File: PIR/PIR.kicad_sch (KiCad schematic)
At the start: 31 parts, among them J1 FLASH, J2 PIR, J3 BUS, J4 Conn_01x04_Socket, Q1 BC846, Q2 BC846, Q3 BC857, SW1 tamper switch, U1 AP63203WU, U2 WT8266-S1

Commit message: upgrades people, upgrades!
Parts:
- added TP8: TestPoint, TestPoint:TestPoint_Pad_1.5x1.5mm, symbol Connector:TestPoint
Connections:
- net +3.3V: now also TP8.1

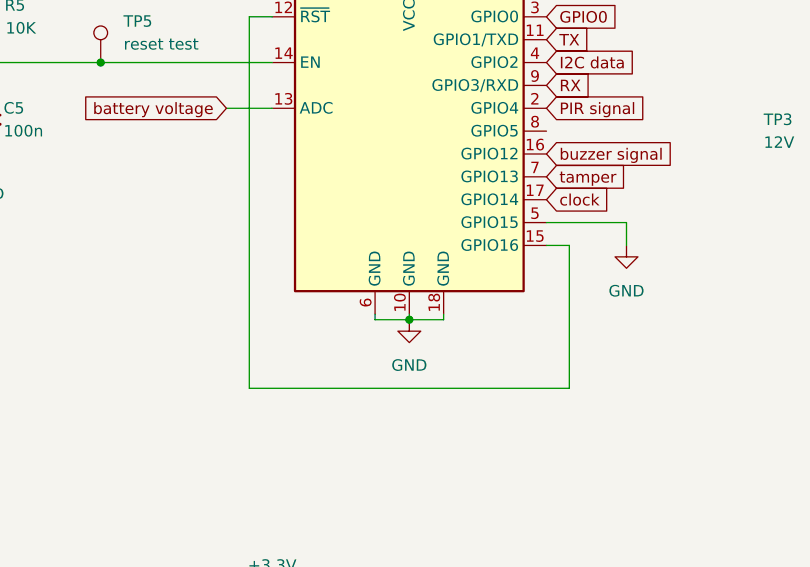
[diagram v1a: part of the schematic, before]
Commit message: Update symbol and footprint of WT8266
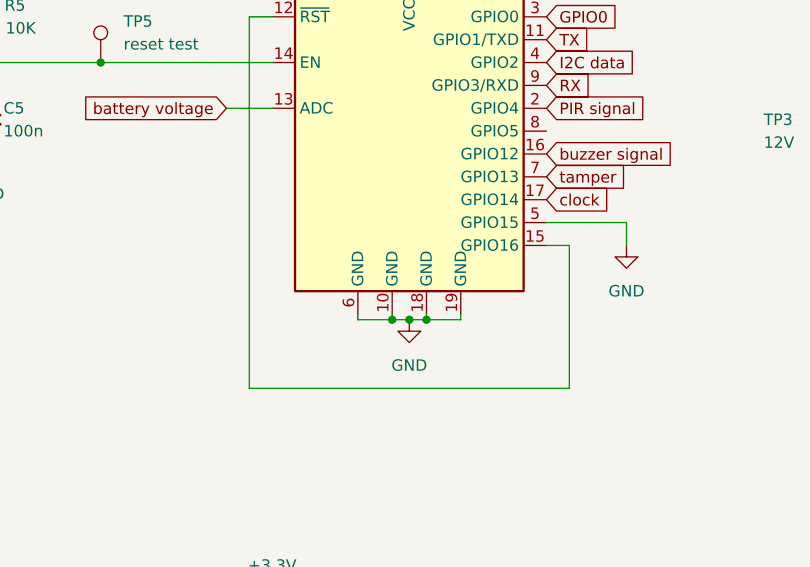
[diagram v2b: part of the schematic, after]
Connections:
- net GND: now also U2.19 (GND)
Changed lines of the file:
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@@
     (company "Radim Kolář, Tomáš Bezányi")
   )
+  (junction (at 94.615 102.235) (diameter 0) (color 0 0 0 0)
+  )
   (junction (at 199.39 121.92) (diameter 0) (color 0 0 0 0)
   )
@@
   (junction (at 144.78 80.01) (diameter 0) (color 0 0 0 0)
   )
+  (junction (at 90.805 102.235) (diameter 0) (color 0 0 0 0)
+  )
   (junction (at 152.4 80.01) (diameter 0) (color 0 0 0 0)
   )
@@
   (junction (at 204.47 82.55) (diameter 0) (color 0 0 0 0)
   )
-  (wire (pts (xy 92.71 101.6) (xy 92.71 102.235))
-    (stroke (width 0) (type default))
-  )
   (wire (pts (xy 160.02 85.09) (xy 152.4 85.09))
     (stroke (width 0) (type default))
@@
     (stroke (width 0) (type default))
   )
+  (wire (pts (xy 90.805 101.6) (xy 90.805 102.235))
+    (stroke (width 0) (type default))
+  )
   (wire (pts (xy 204.47 90.17) (xy 213.36 90.17))
     (stroke (width 0) (type default))
@@
     (stroke (width 0) (type default))
   )
-  (wire (pts (xy 88.9 102.235) (xy 92.71 102.235))
+  (wire (pts (xy 86.995 102.235) (xy 90.805 102.235))
     (stroke (width 0) (type default))
   )
@@
     (stroke (width 0) (type default))
   )
+  (wire (pts (xy 98.425 102.235) (xy 98.425 101.6))
+    (stroke (width 0) (type default))
+  )
   (wire (pts (xy 260.35 40.64) (xy 257.81 40.64))
     (stroke (width 0) (type default))
   )
+  (wire (pts (xy 94.615 102.235) (xy 98.425 102.235))
+    (stroke (width 0) (type default))
+  )
+  (wire (pts (xy 90.805 102.235) (xy 92.71 102.235))
+    (stroke (width 0) (type default))
+  )
   (wire (pts (xy 144.78 80.01) (xy 152.4 80.01))
     (stroke (width 0) (type default))
@@
     (stroke (width 0) (type default))
   )
+  (wire (pts (xy 86.995 102.235) (xy 86.995 101.6))
+    (stroke (width 0) (type default))
+  )
   (wire (pts (xy 204.47 82.55) (xy 213.36 82.55))
     (stroke (width 0) (type default))
@@
     (stroke (width 0) (type default))
   )
+  (wire (pts (xy 94.615 101.6) (xy 94.615 102.235))
+    (stroke (width 0) (type default))
+  )
   (wire (pts (xy 199.39 82.55) (xy 199.39 85.09))
     (stroke (width 0) (type default))
@@
     (stroke (width 0) (type default))
   )
-  (wire (pts (xy 92.71 102.235) (xy 96.52 102.235))
+  (wire (pts (xy 92.71 102.235) (xy 94.615 102.235))
     (stroke (width 0) (type default))
   )
@@
     (stroke (width 0) (type default))
   )
-  (wire (pts (xy 96.52 101.6) (xy 96.52 102.235))
-    (stroke (width 0) (type default))
-  )
   (wire (pts (xy 257.81 40.64) (xy 257.81 48.26))
     (stroke (width 0) (type default))
@@
   )
   (wire (pts (xy 242.57 85.09) (xy 264.16 85.09))
-    (stroke (width 0) (type default))
-  )
-  (wire (pts (xy 88.9 101.6) (xy 88.9 102.235))
     (stroke (width 0) (type default))
   )
@@
       (effects (font (size 1.27 1.27)) hide)
     )
-    (property "Datasheet" "https://botland.cz/index.php?controller=attachment&id_attachment=1796" (at 83.82 81.28 0)
+    (property "Datasheet" "https://web.archive.org/web/20230921181528id_/http://ttcnc.co.kr/wp-content/uploads/2021/05/WT8266-S1-DataSheet-V2.5.pdf" (at 83.82 81.28 0)
       (effects (font (size 1.27 1.27)) hide)
     )
@@
     (pin "17")
     (pin "18")
+    (pin "19")
     (pin "2")
     (pin "3")

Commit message: Fix incident
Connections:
- net at C2.2, L1.1: now also U1.5 (SW); no longer U1.6 (BST)
- net at C2.1: now also U1.6 (BST); no longer U1.5 (SW)
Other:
- moved on the sheet: C1, C2, C3, C4, L1, TP3, U1
